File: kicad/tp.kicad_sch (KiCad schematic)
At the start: 17 parts, among them SW1 SWITCH_MODE, SW2 ALARM_OFF, U1 STM32 NUCLEO F103RB, U2 MAX30102, U3 HM10

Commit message: fix(sch): el symbol tenia asociada una huella incorrecta
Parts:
- U2: footprint Connector_PinHeader_2.54mm:PinHeader_1x06_P2.54mm_Vertical -> Connector_PinHeader_2.54mm:PinHeader_1x07_P2.54mm_Vertical
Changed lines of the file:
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@@
 			)
 		)
-		(property "Footprint" "Connector_PinHeader_2.54mm:PinHeader_1x06_P2.54mm_Vertical"
+		(property "Footprint" "Connector_PinHeader_2.54mm:PinHeader_1x07_P2.54mm_Vertical"
 			(at 56.896 129.032 0)
 			(effects

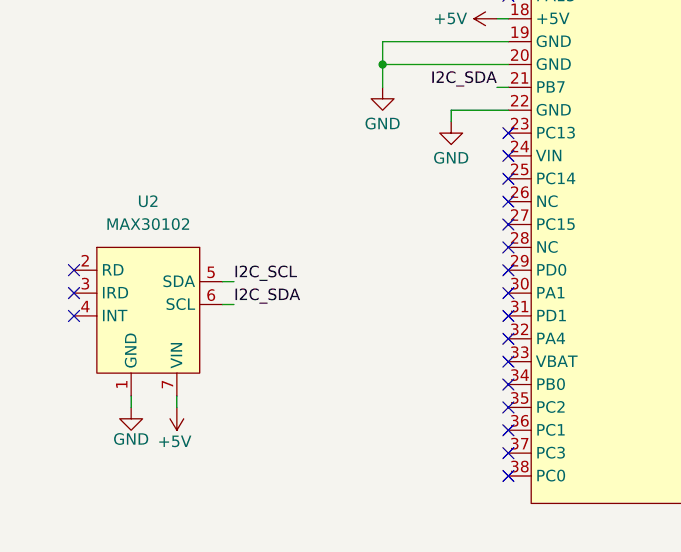
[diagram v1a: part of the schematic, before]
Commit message: fix(sch): actualiza symbol del max30102
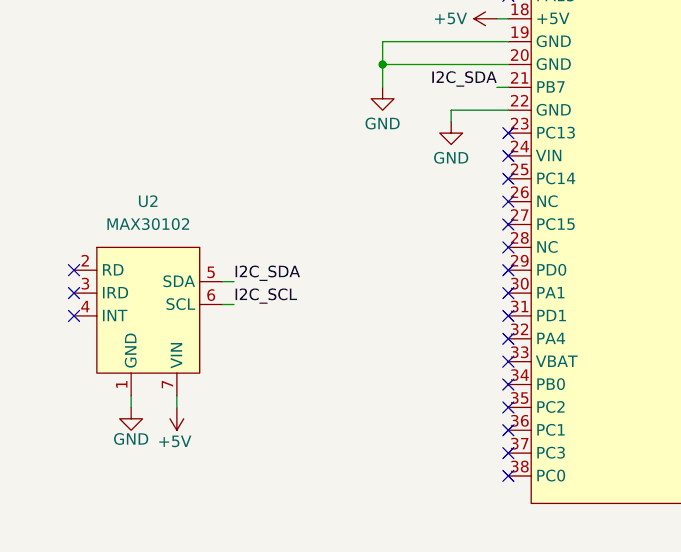
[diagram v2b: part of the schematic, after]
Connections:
- net I2C_SCL: now also U2.6 (SCL); no longer U2.5 (SDA)
- net I2C_SDA: now also U2.5 (SDA); no longer U2.6 (SCL)
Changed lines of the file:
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@@
 	)
 	(label "I2C_SDA"
-		(at 63.5 125.73 0)
+		(at 63.5 123.19 0)
 		(effects
 			(font
@@
 	)
 	(label "I2C_SCL"
-		(at 63.5 123.19 0)
+		(at 63.5 125.73 0)
 		(effects
 			(font

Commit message: style(sch): cambio el footprint por un pinsocket
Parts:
- U2: footprint Connector_PinHeader_2.54mm:PinHeader_1x07_P2.54mm_Vertical -> Connector_PinSocket_2.54mm:PinSocket_1x07_P2.54mm_Vertical
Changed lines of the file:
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@@
 			)
 		)
-		(property "Footprint" "Connector_PinHeader_2.54mm:PinHeader_1x07_P2.54mm_Vertical"
+		(property "Footprint" "Connector_PinSocket_2.54mm:PinSocket_1x07_P2.54mm_Vertical"
 			(at 56.896 129.032 0)
 			(effects
